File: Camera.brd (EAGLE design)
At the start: 30 x 60 mm, 49 parts, among them J1 DM3AT-SF-PEJM5, SW5 THAU13-AB-R, SW6 THAU13-AB-R, SW7 TVAF06-A020B-R, SW8 TVAF06-A020B-R, U4 OPA340N, U5 DRIVER-LV8548MC-AH(SOIC10), U6 I-02247_NJM2845

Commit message: Fix analog input pins
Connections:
- net MSENSE: now also U$2.IO32; no longer U$2.IO12
- net SW1: now also U$2.IO12; no longer U$2.IO13
- net SW2: now also U$2.IO27; no longer U$2.IO35
- net SW3: now also U$2.IO13; no longer U$2.IO14
- net SW4: now also U$2.IO14; no longer U$2.IO32
- net VSENSE: now also U$2.IO35; no longer U$2.IO27
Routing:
- net MSENSE: track 39.9 -> 50.9 mm
- net VSENSE: track 17.7 -> 27.8 mm
- net SW2: track 43.4 -> 38.9 mm, vias 0 -> 2
- net SW1: track 20.5 -> 24.6 mm
- net N$10: track 27.4 -> 31.5 mm
- net SW4: track 28.4 -> 24.5 mm, vias 1 -> 3
- net SW3: track 13.0 -> 9.55 mm
- net J2: track 23.1 -> 24.7 mm
- net J0: track 17.9 -> 19.2 mm
- net J1: track 20.9 -> 22.0 mm
- net GND: track 222.8 -> 222.5 mm, vias 11 -> 9

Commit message: reduce switch pins
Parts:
- removed J1: DM3AT-SF-PEJM5, dm3at-sf-pejm5:HRS_DM3AT-SF-PEJM5
- removed J3, J4, J5: (no value), jumper:SJ
- added R25, R26, R27, R28, R29: (no value), rcl:R0603
- turned SW7 to 180 degrees
- turned SW8 to 180 degrees
- renumbered C10 to C18, C11 to C19, C12 to C20, C7 to C15, C8 to C16, C9 to C17, R10 to R20, R11 to R21, R12 to R22, R13 to R23, R14 to R24, R8 to R18, R9 to R19, U$2 to U$7, U$4 to U$8, U$5 to U$9
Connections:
- removed net J0: J3.1, U$7.IO26
- removed net J1: J4.1, U$7.IO25
- removed net J2: J5.1, U$7.IO33
- removed net SW1: SW6.1, SW6.2, U$7.IO12
- removed net SW2: SW5.1, SW5.2, U$7.IO27
- removed net SW3: SW7.P$1, U$7.IO13
- removed net SW4: SW8.P$1, U$7.IO14
- removed net VSS: J1.6
- new net N$20: R27.1, R28.2, SW5.1, SW5.2, SW7.P$2
- new net N$21: R26.1, R27.2, SW6.3, SW6.4, SW7.P$1
- new net N$22: R28.1, R29.2, SW5.3, SW5.4, SW8.P$1
- new net SW: R25.1, R26.2, SW6.1, SW6.2, U$7.IO34
- net GND: now also R29.1; no longer J3.2, J4.2, J5.2, SW5.3, SW5.4, SW6.3, SW6.4, SW7.P$2
- net VDD: now also R25.2; no longer J1.4
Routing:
- net SW: track 0.00 -> 45.9 mm, vias 0 -> 2
- net N$20: track 0.00 -> 39.0 mm, vias 0 -> 2
- net SW2: track 38.9 -> 0.00 mm, vias 2 -> 0
- net GND: track 222.5 -> 196.6 mm
- net J2: track 24.7 -> 0.00 mm, vias 1 -> 0
- net SW1: track 24.6 -> 0.00 mm
- net SW4: track 24.5 -> 0.00 mm, vias 3 -> 0
- net J1: track 22.0 -> 0.00 mm, vias 1 -> 0
- net J0: track 19.2 -> 0.00 mm, vias 1 -> 0
- net N$22: track 0.00 -> 18.8 mm, vias 0 -> 1
- net N$21: track 0.00 -> 18.5 mm, vias 0 -> 1
- net SW3: track 9.55 -> 0.00 mm, vias 1 -> 0
- net VDD: track 131.7 -> 138.4 mm, vias 7 -> 8
- net MSENSE: track 50.9 -> 47.6 mm
- net VSENSE: track 27.8 -> 25.2 mm
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
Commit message: Camera Unit
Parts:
- added C7: 15pF, rcl:C0603
- added C8: 0.1µF, rcl:C0603
- added R6: 1k, rcl:R0603
- moved R5 42.7 mm to (0.00, 11.4), turned to 90 degrees
- moved R4 39.5 mm to (7.62, 15.2), turned to 90 degrees
- moved R3 37.1 mm to (2.54, 11.4), turned to 90 degrees
- moved C14 36.1 mm to (5.08, 15.2), turned to 270 degrees
- moved C1 35.8 mm to (-6.35, 8.89)
- moved C13 34.1 mm to (7.62, 11.4), turned to 270 degrees
- moved C4 33.0 mm to (-7.62, 15.2), turned to 270 degrees
- moved R1 33.0 mm to (-7.62, 11.4), turned to 90 degrees
- moved R2 31.8 mm to (-5.08, 15.2), turned to 90 degrees
- moved C5 31.4 mm to (2.54, 8.89), turned to 180 degrees
- moved C2 30.7 mm to (-2.54, 8.89)
- moved C3 28.7 mm to (-2.54, 11.4), turned to 270 degrees
- moved C6 25.2 mm to (6.35, 8.89), turned to 180 degrees
- moved U$3 6.35 mm to (-5.08, 11.4)
- moved U$6 5.08 mm to (5.08, 11.4)
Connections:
- removed net AGND: U$1.23
- removed net DGND: U$1.10
- removed net DOVDD: U$1.14
- removed net SPI_CLK: U$7.IO18
- removed net SPI_CS: U$7.IO5
- removed net SPI_MISO: U$7.IO19
- new net CAM_RESET: U$1.19, U$7.IO14
- new net D0: U$1.6, U$7.IO5
- new net D1: U$1.4, U$7.IO19
- new net D2: U$1.3, U$7.IO23
- new net D3: U$1.5, U$7.IO18
- new net D4: U$1.7, U$7.IO27
- new net D5: U$1.9, U$7.IO33
- new net D6: U$1.11, U$7.SENSOR_VN
- new net D7: U$1.13, U$7.SENSOR_VP
- new net HSYNC: U$1.16, U$7.IO26
- new net N$10: U$7.IO13
- new net N$7: R6.1, U$1.17
- new net PCLK: C7.1, U$1.8
- new net VSYNC: U$1.18, U$7.IO12
- new net XCLK: U$1.12, U$7.IO25
- net GND: now also C7.2, C8.2, R6.2, U$1.10, U$1.23, U$1.PAD1, U$1.PAD2
- net I2C_SCL: now also U$1.20
- net I2C_SDA: now also U$1.22
- net VDD: now also C8.1, U$1.14
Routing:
- net GND: track 196.6 -> 255.5 mm, vias 9 -> 11
- net VDD: track 138.4 -> 192.6 mm, vias 8 -> 10
- net D4: track 0.00 -> 31.5 mm, vias 0 -> 3
- net VSYNC: track 0.00 -> 31.3 mm, vias 0 -> 3
- net HSYNC: track 0.00 -> 29.5 mm, vias 0 -> 3
- net CAM_RESET: track 0.00 -> 28.5 mm, vias 0 -> 3
- net 1.3V: track 0.00 -> 26.9 mm
- net XCLK: track 0.00 -> 26.3 mm, vias 0 -> 3
- net I2C_SDA: track 0.00 -> 26.1 mm, vias 0 -> 1
- net D5: track 0.00 -> 26.0 mm, vias 0 -> 3
- net I2C_SCL: track 0.00 -> 22.9 mm, vias 0 -> 1
- net 2.8V: track 0.00 -> 22.8 mm
- net D0: track 0.00 -> 20.7 mm, vias 0 -> 1
- net D3: track 0.00 -> 19.2 mm, vias 0 -> 1
- net D6: track 0.00 -> 19.0 mm, vias 0 -> 1
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
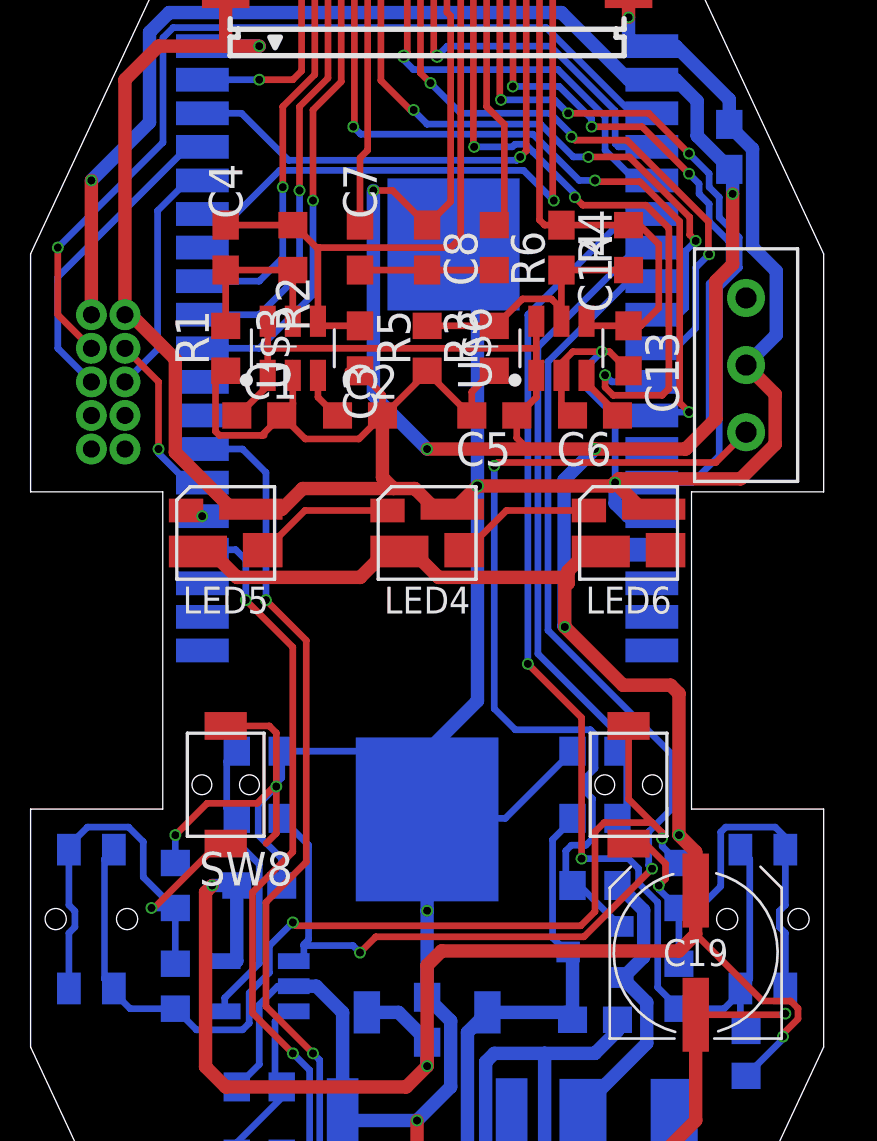
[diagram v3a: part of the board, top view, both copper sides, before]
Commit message: change parts name
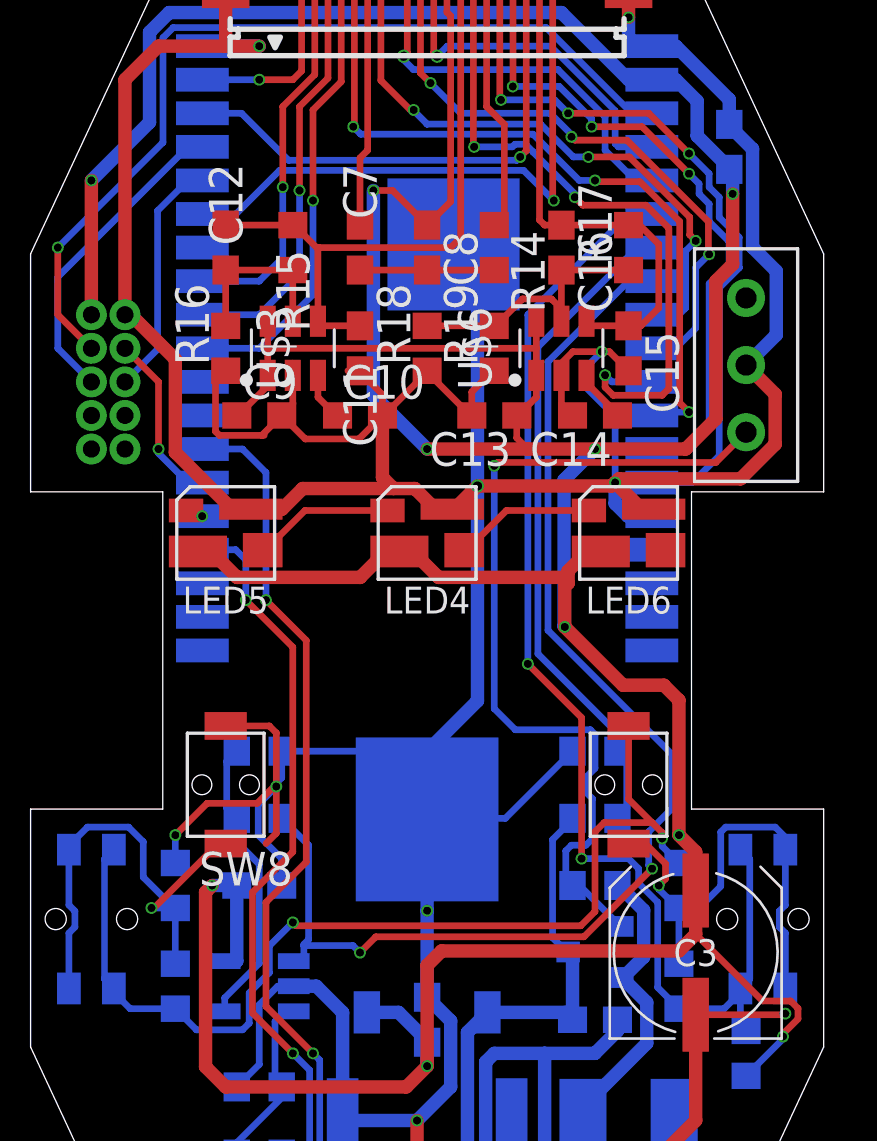
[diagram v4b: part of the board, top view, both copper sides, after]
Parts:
- removed C17: 0.33µF, rcl:C0603
- removed C18: 2.2µF, rcl:C0603
- removed C19: 220µF, rcl:UD-6,3X7,7_NICHICON
- removed C20: 0.1µF, rcl:C0603
- removed R20: 1k, rcl:R0603
- removed R22: 200k, rcl:R0603
- removed R23, R24: 100k, rcl:R0603
- removed RS1: 20m, rcl:R6332W
- added C10: 0.01µF, resistor:C0603
- added C11: 2.2µF, resistor:C0603
- added C12: 100pF, resistor:C0603
- added C9: 0.1µF, resistor:C0603
- added R14: 1k, rcl:R0603
- added R15, R17: 10k, resistor:R0603
- added R16: 100k, resistor:R0603
- added R8: 100k, rcl:R0603
- C1: value 0.1µF -> 0.33µF; device resistor:C0603 -> rcl:C0603
- C13: value 1.0µF -> 0.1µF
- C14: value 100pF -> 0.01µF
- C15: value 0.1µF -> 1.0µF; device rcl:C0603 -> resistor:C0603
- C16: value 1µF -> 100pF; device rcl:C0603 -> resistor:C0603
- C2: value 0.01µF -> 2.2µF; device resistor:C0603 -> rcl:C0603
- C3: value 2.2µF -> 220µF; device resistor:C0603 -> rcl:UD-6,3X7,7_NICHICON
- C4: value 100pF -> 0.1µF; device resistor:C0603 -> rcl:C0603
- C5: value 0.1µF -> 1µF; device resistor:C0603 -> rcl:C0603
- C6: value 0.01µF -> 0.1µF; device resistor:C0603 -> rcl:C0603
- R1: device resistor:R0603 -> rcl:R0603
- R18: value 1k -> 47k; device rcl:R0603 -> resistor:R0603
- R19: value 100k -> 10k; device rcl:R0603 -> resistor:R0603
- R2: value 10k -> 200k; device resistor:R0603 -> rcl:R0603
- R3: value 10k -> 100k; device resistor:R0603 -> rcl:R0603
- R4: value 10k -> 1k; device resistor:R0603 -> rcl:R0603
- R5: value 47k -> 20m; device resistor:R0603 -> rcl:R6332W
- moved C16 37.2 mm to (5.08, 15.2), flipped to the top, turned to 270 degrees
- moved R4 37.0 mm to (-6.35, -19.1), flipped to the bottom, turned to 0 degrees
- moved C5 30.6 mm to (0.00, -21.6), flipped to the bottom, turned to 0 degrees
- moved R5 29.2 mm to (0.00, -17.8), flipped to the bottom, turned to 180 degrees
- moved C1 26.2 mm to (6.35, -14.0), flipped to the bottom, turned to 180 degrees
- moved C3 26.2 mm to (10.2, -11.4), turned to 90 degrees
- moved C15 24.7 mm to (7.62, 11.4), flipped to the top, turned to 270 degrees
- moved R1 24.7 mm to (6.35, -8.89), flipped to the bottom, turned to 180 degrees
- moved R2 24.4 mm to (6.35, -6.35), flipped to the bottom, turned to 0 degrees
- moved C2 23.0 mm to (0.00, -14.0), flipped to the bottom, turned to 90 degrees
- moved C6 21.8 mm to (-6.35, -8.89), flipped to the bottom
- moved R6 21.0 mm to (-6.35, -3.81), flipped to the bottom, turned to 0 degrees
- moved R19 19.9 mm to (2.54, 11.4), flipped to the top, turned to 90 degrees
- moved C4 19.4 mm to (11.4, 19.1), flipped to the bottom, turned to 90 degrees
- moved R18 16.5 mm to (0.00, 11.4), flipped to the top, turned to 90 degrees
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- renumbered R21 to R7, R25 to R9, R26 to R10, R27 to R11, R28 to R12, R29 to R13
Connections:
- net 1.3V: now also C11.1, C12.1, R15.2; no longer C3.1, C4.1, R2.2
- net 2.8V: now also C15.1, C16.1, R17.2; no longer C13.1, C14.1, R4.2
- net GND: now also C10.2, C11.2, C14.2, C3.-, C4.2, C5.1, C9.2, R14.2, R16.1, R19.1, R6.1; no longer C16.1, C17.2, C18.2, C19.-, C20.2, C3.2, C5.2, R1.1, R23.1, R6.2, RS1.1
- net MGND: now also R4.1, R5.2; no longer R20.1, RS1.2
- net MSENSE: now also R8.2; no longer R19.2
- net N$1: now also C10.1; no longer C2.1
- net N$14: now also R1.2; no longer R24.2
- net N$15: now also R6.2, R8.1; no longer R18.2, R19.1
- net N$16: now also R4.2; no longer R20.2
- net N$17: now also R1.1; no longer R24.1
- net N$2: now also C12.2, R15.1, R16.2; no longer C4.2, R1.2, R2.1
- net N$3: now also C14.1; no longer C6.1
- net N$4: now also C16.2, R17.1, R18.2, R19.2; no longer C14.2, R3.2, R4.1, R5.2
- net N$7: now also R14.1; no longer R6.1
- net VCC: now also C1.1, C5.2, R2.2; no longer C16.2, C17.1, R22.2
- net VDD: now also C13.1, C2.1, C3.+, C4.1, C6.1, C9.1; no longer C1.1, C15.1, C18.1, C19.+, C20.1, C5.1
- net VSENSE: now also R2.1, R3.2; no longer R22.1, R23.2

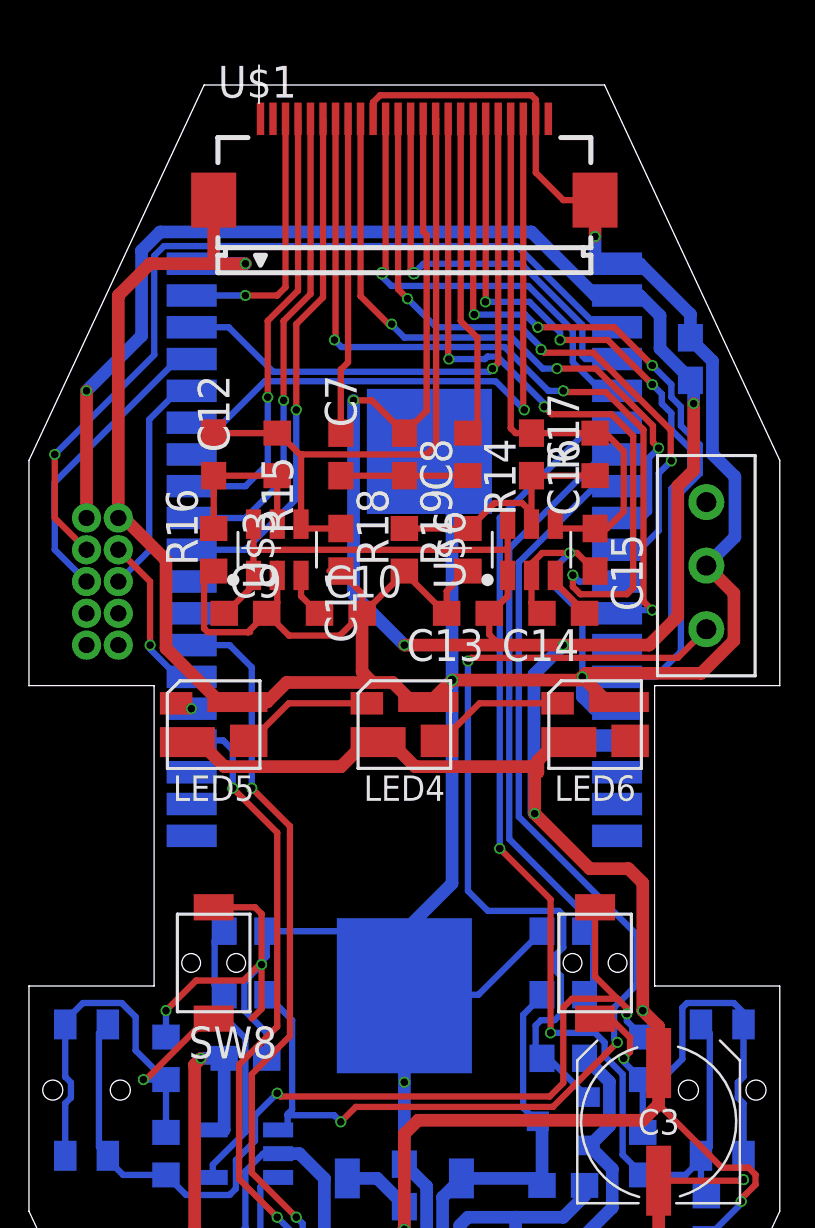
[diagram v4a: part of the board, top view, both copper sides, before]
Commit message: Format silk
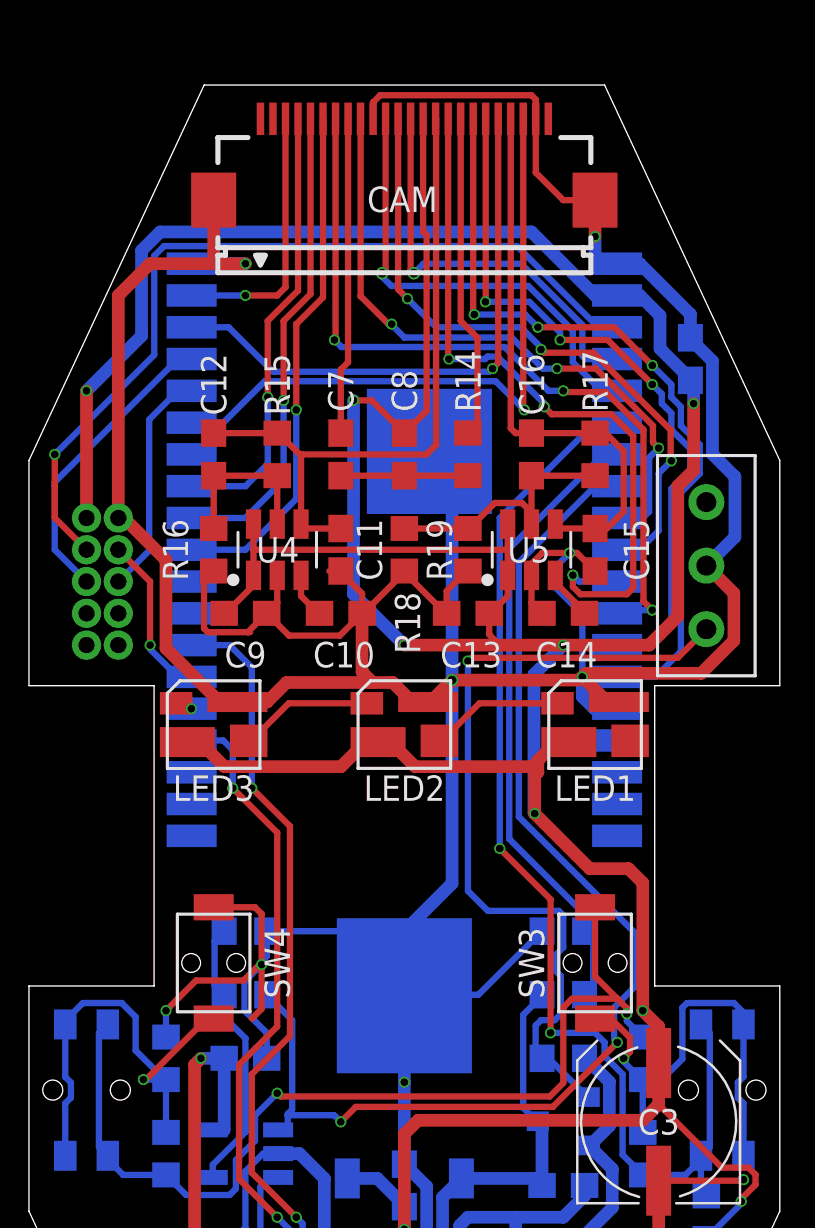
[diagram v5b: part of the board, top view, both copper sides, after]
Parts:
- removed U$3, U$6: NJM11100, regulators:SOT95P240X110-6N
- added U2: DRIVER-LV8548MC-AH(SOIC10), DRIVER-LV8548MC-AH_SOIC10_:SOIC10-1.0-5X4MM
- added U3: OPA340N, burr-brown:SOT23-5
- U4: value OPA340N -> NJM11100; device burr-brown:SOT23-5 -> regulators:SOT95P240X110-6N
- U5: value DRIVER-LV8548MC-AH(SOIC10) -> NJM11100; device DRIVER-LV8548MC-AH_SOIC10_:SOIC10-1.0-5X4MM -> regulators:SOT95P240X110-6N
- moved U5 37.2 mm to (5.08, 11.4), flipped to the top
- moved U4 24.2 mm to (-5.08, 11.4), flipped to the top, turned to 90 degrees
- renumbered LED4 to LED2, LED5 to LED3, LED6 to LED1, SW5 to SW2, SW6 to SW1, SW7 to SW3, SW8 to SW4, U$1 to CAM, U$7 to ESP32, U6 to U1
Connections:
- net 1.3V: now also U4.4; no longer U$3.4
- net 2.8V: now also U5.4; no longer U$6.4
- net GND: now also U3.2, U5.2; no longer U$3.2, U$6.2
- net M1: now also U2.10, U2.8; no longer U5.10, U5.8
- net M2: now also U2.7, U2.9; no longer U5.7, U5.9
- net MC1: now also U2.2, U2.4; no longer U5.2, U5.4
- net MC2: now also U2.3, U2.5; no longer U5.3, U5.5
- net MGND: now also U2.6; no longer U5.6
- net MSENSE: now also U3.1; no longer U4.1
- net N$1: now also U4.3; no longer U$3.3
- net N$15: now also U3.4; no longer U4.4
- net N$16: now also U3.3; no longer U4.3
- net N$2: now also U4.5; no longer U$3.5
- net N$3: now also U5.3; no longer U$6.3
- net N$4: now also U5.5; no longer U$6.5
- net VCC: now also U2.1; no longer U5.1
- net VDD: now also U3.5, U4.1, U4.6, U5.1, U5.6; no longer U$3.1, U$3.6, U$6.1, U$6.6, U4.5
